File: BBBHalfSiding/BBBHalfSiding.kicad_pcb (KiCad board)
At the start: 2 copper layers, 54.6 x 86.4 mm, 2 parts, among them P8 BeagleBone_Black_Header, P9 BeagleBone_Black_Header

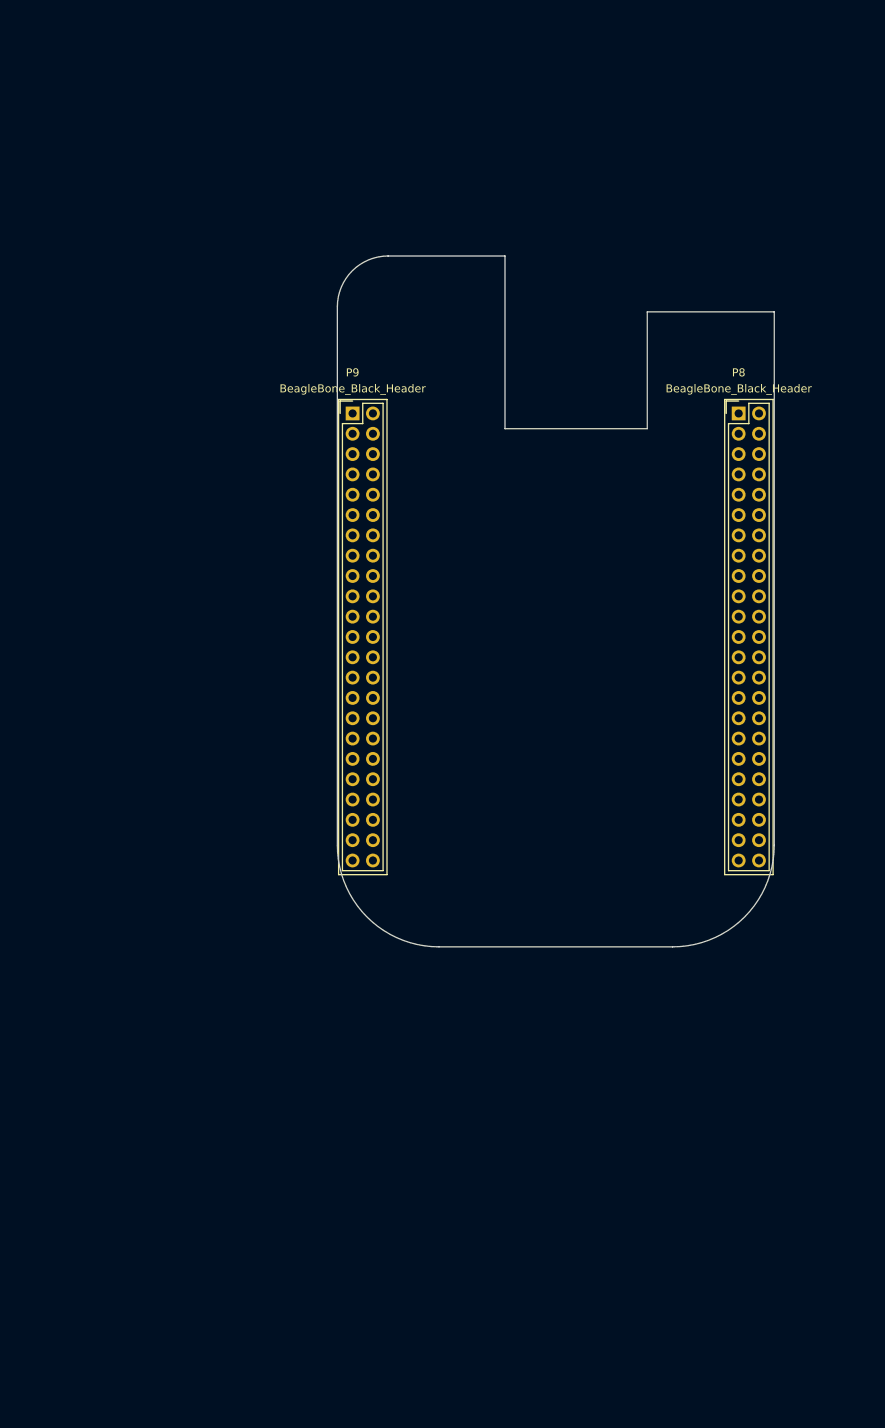
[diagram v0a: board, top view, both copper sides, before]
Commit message: Completed Beagle Bone Black Half Siding Cape
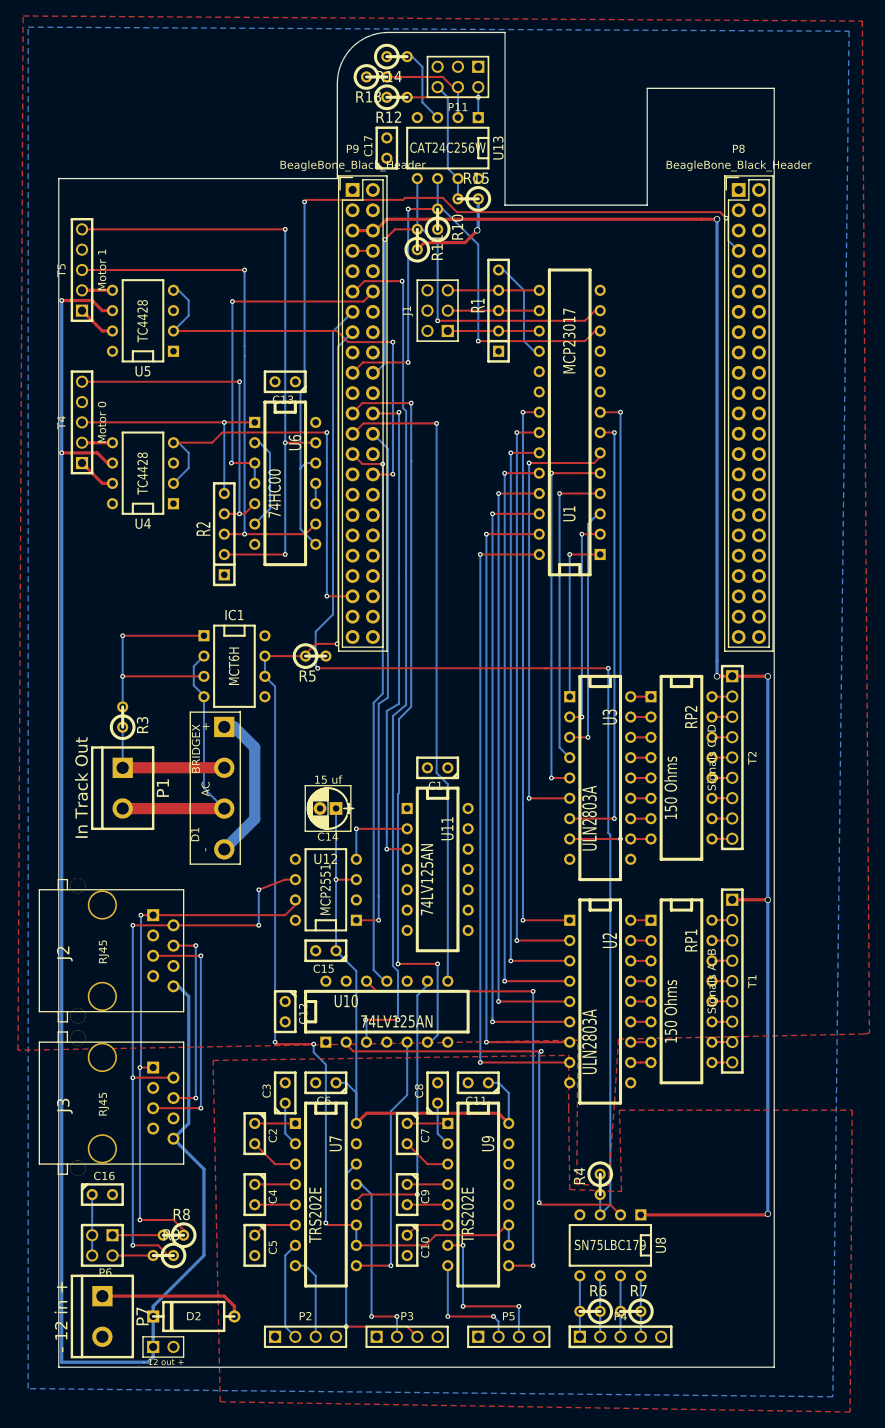
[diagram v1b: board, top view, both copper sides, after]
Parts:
- added C1: .1 uf, C1, F.Cu at (127.0, 106.7)
- added C10: .1 uf, C1, F.Cu at (123.2, 166.4)
- added C11: .1 uf, C1, F.Cu at (132.1, 146.1)
- added C12: .1 uf, C1, F.Cu at (108.0, 137.2)
- added C13: .1 uf, C1, F.Cu at (108.0, 58.4)
- added C14: 15 uf, CP_Radial_D5.0mm_P2.00mm, F.Cu at (114.3, 111.8)
- added C15: .1 uf, C1, F.Cu at (113.0, 129.5)
- added C16: 47 nf, C1, F.Cu at (85.1, 160.0)
- added C17: .1 uf, C1, F.Cu at (120.7, 29.2)
- added C2: .1 uf, C1, F.Cu at (104.1, 152.4)
- added C3: .1 uf, C1, F.Cu at (108.0, 147.3)
- added C4: .1 uf, C1, F.Cu at (104.1, 160.0)
- added C5: .1 uf, C1, F.Cu at (104.1, 166.4)
- added C6: .1 uf, C1, F.Cu at (113.0, 146.1)
- added C7: .1 uf, C1, F.Cu at (123.2, 152.4)
- added C8: .1 uf, C1, F.Cu at (127.0, 147.3)
- added C9: .1 uf, C1, F.Cu at (123.2, 160.0)
- added D1: BRIDGEX, KBL, F.Cu at (100.3, 109.2)
- added D2: SB240E, DO-15, F.Cu at (96.5, 175.3)
- added IC1: MCT6H, DIP-8__300, F.Cu at (101.6, 94.0)
- added J1: Address, pin_array_3x2, F.Cu at (127.0, 49.5)
- added J2: RJ45, RJ45_8N-S, F.Cu at (85.1, 129.5)
- added J3: RJ45, RJ45_8N-S, F.Cu at (85.1, 148.6)
- added P1: In Track Out, bornier2, F.Cu at (87.6, 109.2)
- added P10: - 12 out +, ScrewTerm2.54-2, F.Cu at (92.7, 179.1)
- added P11: addr / we, pin_array_3x2, F.Cu at (129.5, 20.3)
- added P2: East (Points), PIN_ARRAY_4x1, F.Cu at (110.5, 177.8)
- added P3: West Main (Frog, Normal), PIN_ARRAY_4x1, F.Cu at (123.2, 177.8)
- added P4: ABS Slave Bus, PIN_ARRAY_5x1, F.Cu at (149.9, 177.8)
- added P5: West Div. (Frog, Revesed), PIN_ARRAY_4x1, F.Cu at (135.9, 177.8)
- added P6: Termination, PIN_ARRAY_2X2, F.Cu at (85.1, 166.4)
- added P7: - 12 in +, bornier2, F.Cu at (85.1, 175.3)
- added R1: 10K Ohms, SIL-5, F.Cu at (134.6, 48.3)
- added R10: 5.6K Ohms, R1, F.Cu at (127.0, 38.1)
- added R11: 5.6K Ohms, R1, F.Cu at (124.5, 40.6)
- added R12: 4.75K Ohms, R1, F.Cu at (121.9, 22.9)
- added R13: 4.75K Ohms, R1, F.Cu at (119.4, 20.3)
- added R14: 4.75K Ohms, R1, F.Cu at (121.9, 17.8)
- added R15: 10K Ohms, R1, F.Cu at (130.8, 35.6)
- added R2: 10K Ohms, SIL-5, F.Cu at (100.3, 76.2)
- added R3: 10 Ohms, R1, F.Cu at (87.6, 100.3)
- added R4: 10K Ohms, R1, F.Cu at (147.3, 158.8)
- added R5: 10K Ohms, R1, F.Cu at (111.8, 92.7)
- added R6: 60 Ohms, R1, F.Cu at (146.1, 174.6)
- added R7: 60 Ohms, R1, F.Cu at (151.1, 174.6)
- added R8: 60 Ohms, R1, F.Cu at (94.0, 165.1)
- added R9: 60 Ohms, R1, F.Cu at (92.7, 167.6)
- added RP1: 150 Ohms, DIP-16__300, F.Cu at (157.5, 134.6)
- added RP2: 150 Ohms, DIP-16__300, F.Cu at (157.5, 106.7)
- added T1: Signals A, B, ScrewTerm_2.54-9, F.Cu at (163.8, 133.3)
- added T2: Signals C, D, ScrewTerm_2.54-9, F.Cu at (163.8, 105.4)
- added T4: Motor 0, ScrewTerm_2.54-5, F.Cu at (82.5, 63.5)
- added T5: Motor 1, ScrewTerm_2.54-5, F.Cu at (82.5, 44.5)
- added U1: MCP23017, DIP-28__300, F.Cu at (143.5, 63.5)
- added U10: 74LV125AN, DIP-14__300, F.Cu at (120.7, 137.2)
- added U11: 74LV125AN, DIP-14__300, F.Cu at (127.0, 119.4)
- added U12: MCP2551, DIP-8__300, F.Cu at (113.0, 121.9)
- added U13: CAT24C256W, DIP-8__300, F.Cu at (128.3, 29.2)
- added U2: ULN2803A, DIP-18__300, F.Cu at (147.3, 135.9)
- added U3: ULN2803A, DIP-18__300, F.Cu at (147.3, 108.0)
- added U4: TC4428, DIP-8__300, F.Cu at (90.2, 69.8)
- added U5: TC4428, DIP-8__300, F.Cu at (90.2, 50.8)
- added U6: 74HC00, DIP-14__300, F.Cu at (108.0, 71.1)
- added U7: TRS202E, DIP-16__300, F.Cu at (113.0, 160.0)
- added U8: SN75LBC179, DIP-8__300, F.Cu at (148.6, 166.4)
- added U9: TRS202E, DIP-16__300, F.Cu at (132.1, 160.0)
- moved P8 27.9 mm to (164.6, 34.4)
- moved P9 27.9 mm to (116.4, 34.4)
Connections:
- net +3V3 renamed +3.3V
- net GNDD renamed GND
- P8 pad 10: Net-(P8-Pad10) -> (no net)
- P8 pad 11: Net-(P8-Pad11) -> (no net)
- P8 pad 12: Net-(P8-Pad12) -> (no net)
- P8 pad 13: Net-(P8-Pad13) -> (no net)
- P8 pad 14: Net-(P8-Pad14) -> (no net)
- P8 pad 15: Net-(P8-Pad15) -> (no net)
- P8 pad 16: Net-(P8-Pad16) -> (no net)
- P8 pad 17: Net-(P8-Pad17) -> (no net)
- P8 pad 18: Net-(P8-Pad18) -> (no net)
- P8 pad 19: Net-(P8-Pad19) -> (no net)
- P8 pad 20: Net-(P8-Pad20) -> (no net)
- P8 pad 21: Net-(P8-Pad21) -> (no net)
- P8 pad 22: Net-(P8-Pad22) -> (no net)
- P8 pad 23: Net-(P8-Pad23) -> (no net)
- P8 pad 24: Net-(P8-Pad24) -> (no net)
- P8 pad 25: Net-(P8-Pad25) -> (no net)
- P8 pad 26: Net-(P8-Pad26) -> (no net)
- P8 pad 27: Net-(P8-Pad27) -> (no net)
- P8 pad 28: Net-(P8-Pad28) -> (no net)
- P8 pad 29: Net-(P8-Pad29) -> (no net)
- P8 pad 3: Net-(P8-Pad3) -> (no net)
- P8 pad 30: Net-(P8-Pad30) -> (no net)
- P8 pad 31: Net-(P8-Pad31) -> (no net)
- P8 pad 32: Net-(P8-Pad32) -> (no net)
- P8 pad 33: Net-(P8-Pad33) -> (no net)
- P8 pad 34: Net-(P8-Pad34) -> (no net)
- P8 pad 35: Net-(P8-Pad35) -> (no net)
- P8 pad 36: Net-(P8-Pad36) -> (no net)
- P8 pad 37: Net-(P8-Pad37) -> (no net)
- P8 pad 38: Net-(P8-Pad38) -> (no net)
- P8 pad 39: Net-(P8-Pad39) -> (no net)
- P8 pad 4: Net-(P8-Pad4) -> (no net)
- P8 pad 40: Net-(P8-Pad40) -> (no net)
- P8 pad 41: Net-(P8-Pad41) -> (no net)
- P8 pad 42: Net-(P8-Pad42) -> (no net)
- P8 pad 43: Net-(P8-Pad43) -> (no net)
- P8 pad 44: Net-(P8-Pad44) -> (no net)
- P8 pad 45: Net-(P8-Pad45) -> (no net)
- P8 pad 46: Net-(P8-Pad46) -> (no net)
- P8 pad 5: Net-(P8-Pad5) -> (no net)
- P8 pad 6: Net-(P8-Pad6) -> (no net)
- P8 pad 7: Net-(P8-Pad7) -> /M1_Sense
- P8 pad 8: Net-(P8-Pad8) -> (no net)
- P8 pad 9: Net-(P8-Pad9) -> (no net)
- P9 pad 10: SYS_RESETN -> (no net)
- P9 pad 11: Net-(P9-Pad11) -> /Sensors/RX
- P9 pad 12: Net-(P9-Pad12) -> /M0_Sense
- P9 pad 13: Net-(P9-Pad13) -> /Sensors/TX
- P9 pad 14: Net-(P9-Pad14) -> (no net)
- P9 pad 15: Net-(P9-Pad15) -> /Sensors/Occupancy
- P9 pad 16: Net-(P9-Pad16) -> (no net)
- P9 pad 17: Net-(P9-Pad17) -> (no net)
- P9 pad 18: Net-(P9-Pad18) -> (no net)
- P9 pad 19: Net-(P9-Pad19) -> /Signals/SCL
- P9 pad 20: Net-(P9-Pad20) -> /Signals/SDA
- P9 pad 21: Net-(P9-Pad21) -> (no net)
- P9 pad 22: Net-(P9-Pad22) -> (no net)
- P9 pad 23: Net-(P9-Pad23) -> /Sensors/East (Points) Occ
- P9 pad 24: Net-(P9-Pad24) -> /CANBUSDriver/CANRX
- P9 pad 25: Net-(P9-Pad25) -> /Sensors/West Main (Frog Normal) Occ
- P9 pad 26: Net-(P9-Pad26) -> /CANBUSDriver/CANTX
- P9 pad 27: Net-(P9-Pad27) -> /Sensors/West Diverg (Frog Reversed) Occ
- P9 pad 28: Net-(P9-Pad28) -> (no net)
- P9 pad 29: Net-(P9-Pad29) -> (no net)
- P9 pad 30: Net-(P9-Pad30) -> /M1_Control
- P9 pad 31: Net-(P9-Pad31) -> (no net)
- P9 pad 32: VDD_ADC -> (no net)
- P9 pad 33: Net-(P9-Pad33) -> (no net)
- P9 pad 34: GNDA_ADC -> (no net)
- P9 pad 35: Net-(P9-Pad35) -> (no net)
- P9 pad 36: Net-(P9-Pad36) -> (no net)
- P9 pad 37: Net-(P9-Pad37) -> (no net)
- P9 pad 38: Net-(P9-Pad38) -> (no net)
- P9 pad 39: Net-(P9-Pad39) -> (no net)
- P9 pad 40: Net-(P9-Pad40) -> (no net)
- P9 pad 41: Net-(P9-Pad41) -> /M0_Control
- P9 pad 42: Net-(P9-Pad42) -> (no net)
- P9 pad 9: PWR_BUT -> (no net)
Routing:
- net +5V: track 0.00 -> 274.3 mm, vias 0 -> 6
- net +12V: track 0.00 -> 210.7 mm, vias 0 -> 2
- net /Sensors/Occupancy: track 0.00 -> 155.4 mm, vias 0 -> 4
- net /Sensors/TX: track 0.00 -> 154.4 mm, vias 0 -> 2
- net /Sensors/RX: track 0.00 -> 107.3 mm, vias 0 -> 3
- net /M1_Sense: track 0.00 -> 104.8 mm, vias 0 -> 2
- net /Sensors/East (Points) Occ: track 0.00 -> 94.6 mm, vias 0 -> 3
- net /Signals/GP0-7: track 0.00 -> 82.0 mm, vias 0 -> 2
- net /Sensors/West Main (Frog Normal) Occ: track 0.00 -> 81.3 mm, vias 0 -> 1
- net /Signals/GP0-6: track 0.00 -> 80.5 mm, vias 0 -> 2
- net /Signals/GP0-5: track 0.00 -> 79.0 mm, vias 0 -> 2
- net N-0000072: track 0.00 -> 77.5 mm, vias 0 -> 3
- net /Signals/GP0-4: track 0.00 -> 77.5 mm, vias 0 -> 2
- net /Signals/GP0-3: track 0.00 -> 75.9 mm, vias 0 -> 2
- net N-00000206: track 0.00 -> 75.7 mm, vias 0 -> 5
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- added copper zone on F.Cu, net +3.3V
- added copper zone on F.Cu, net +5V
- added copper zone on B.Cu, net GND
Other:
- board size 54.6 x 86.4 mm -> 89.4 x 166.9 mm

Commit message: Updates to BBBHalfSiding (silk screen tweaks)
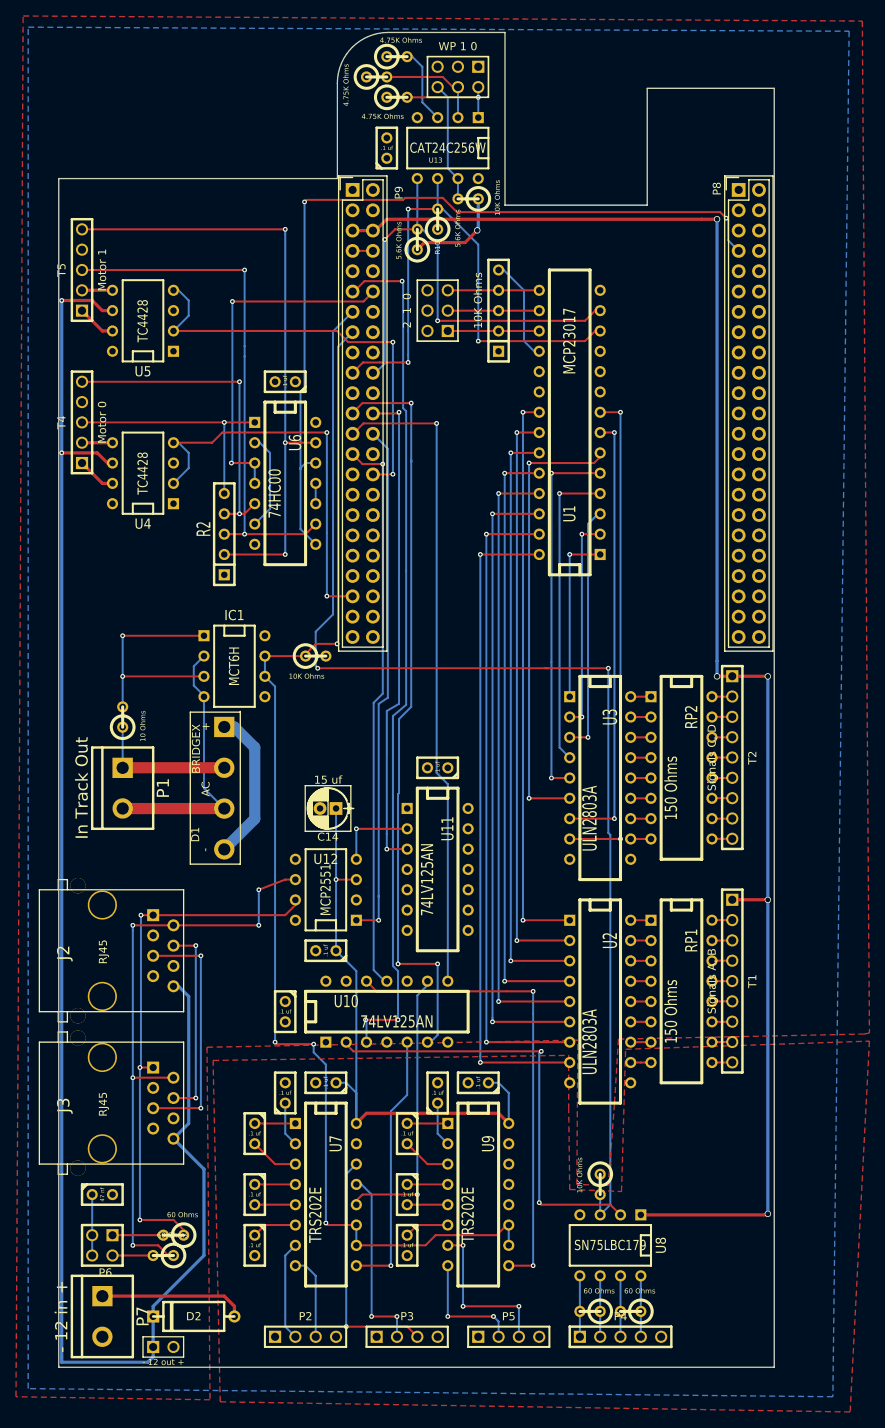
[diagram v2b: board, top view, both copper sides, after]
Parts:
- J1: value Address -> 2 1 0
- P11: value addr / we -> WP 1 0

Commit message: Add missing bypass caps.
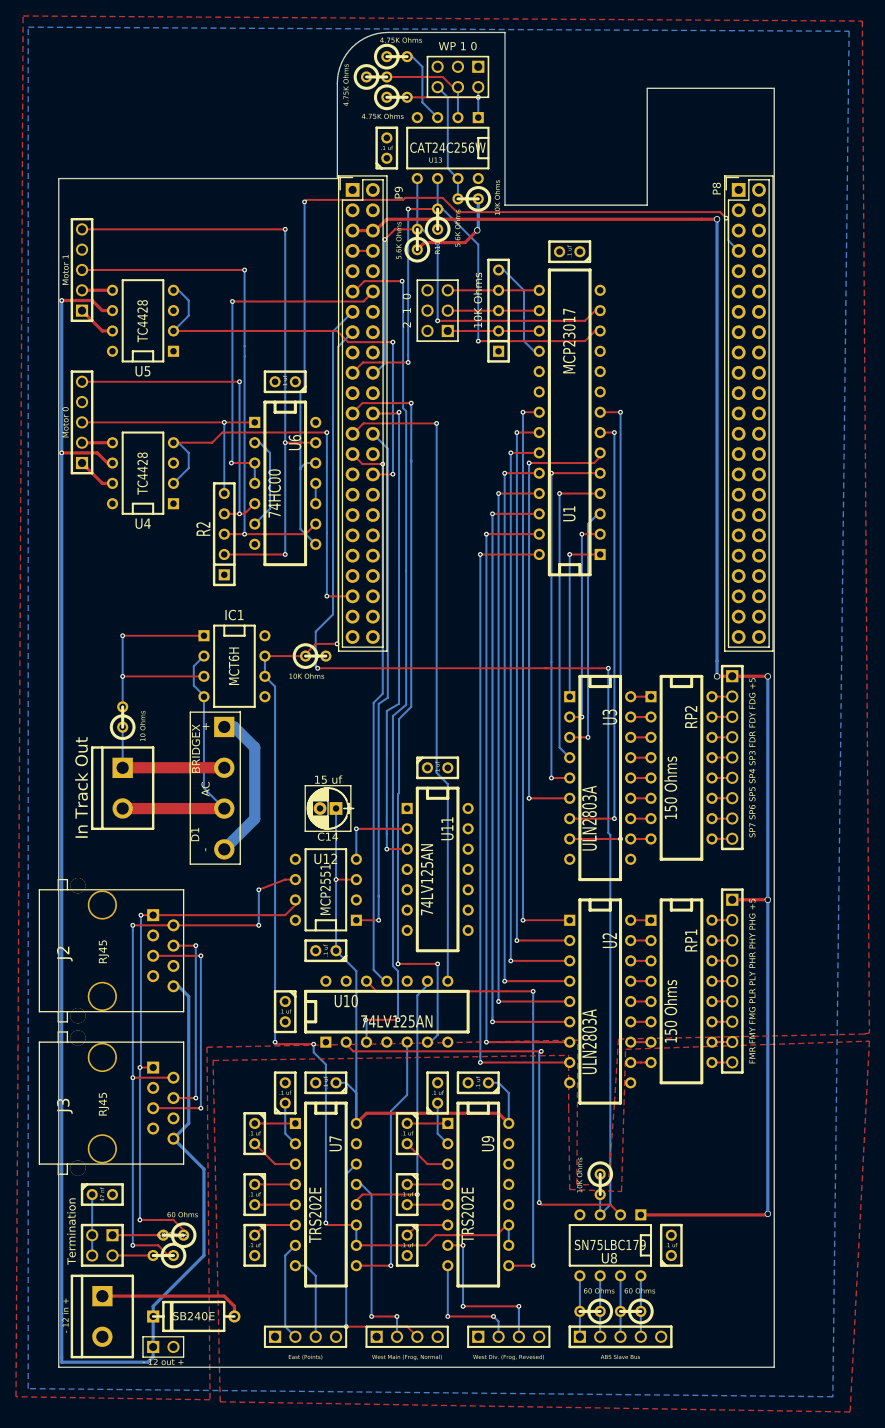
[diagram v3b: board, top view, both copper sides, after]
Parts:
- added C18: .1 uf, C1, F.Cu at (156.2, 166.4)
- added C19: .1 uf, C1, F.Cu at (127.0, 106.7)
- T1: value Signals A, B -> FMR FMY FMG PLR PLY PHR PHY PHG +5
- T2: value Signals C, D -> SP7 SP6 SP5 SP4 SP3 FDR FDY FDG +5
- moved C1 66.6 mm to (143.5, 42.2)

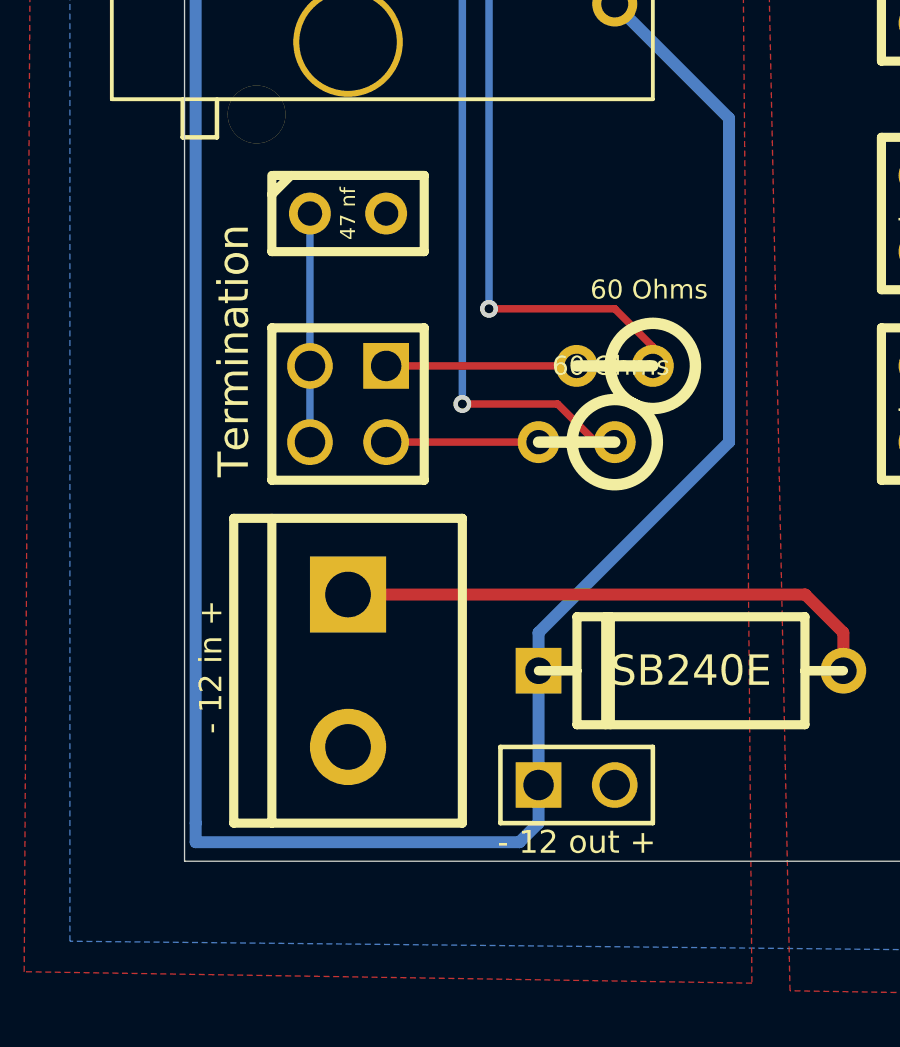
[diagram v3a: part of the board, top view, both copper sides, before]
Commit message: Tweaks to the silk screen for BBBHalfSiding cape.
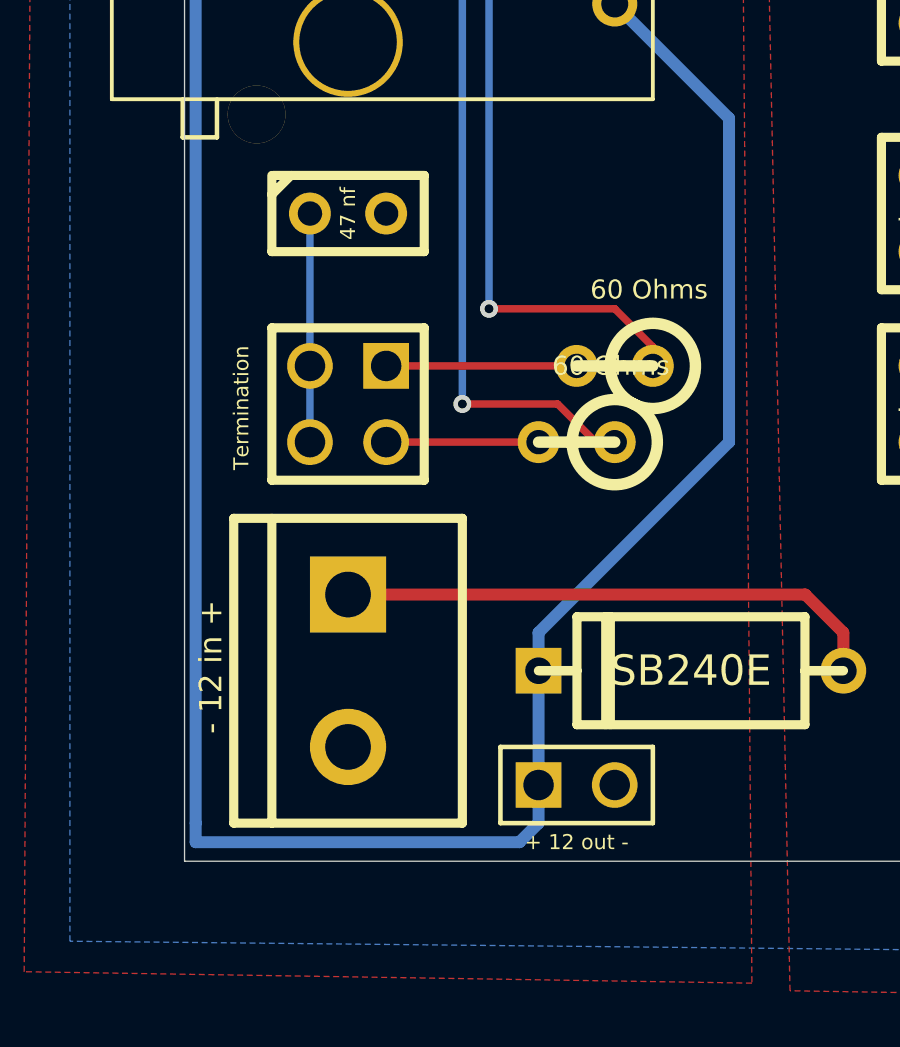
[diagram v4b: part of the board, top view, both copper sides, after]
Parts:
- P10: value - 12 out + -> + 12 out -
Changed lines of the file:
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@@
       (effects (font (size 0.762 0.762) (thickness 0.1524)))
     )
-    (fp_text value "- 12 out +" (at 0 1.905) (layer F.SilkS)
-      (effects (font (size 0.762 0.762) (thickness 0.1524)))
+    (fp_text value "+ 12 out -" (at 0 1.905) (layer F.SilkS)
+      (effects (font (size 0.5 0.5) (thickness 0.1016)))
     )
     (fp_line (start -2.54 1.27) (end -2.54 -1.27) (layer F.SilkS) (width 0.1524))
@@
       (effects (font (size 1.016 1.016) (thickness 0.2032)))
     )
-    (fp_text value Termination (at 3.81 1.778 270) (layer F.SilkS)
-      (effects (font (size 1.016 1.016) (thickness 0.2032)))
+    (fp_text value Termination (at 3.556 -0.127 270) (layer F.SilkS)
+      (effects (font (size 0.5 0.5) (thickness 0.1016)))
     )
     (fp_line (start -2.54 -2.54) (end 2.54 -2.54) (layer F.SilkS) (width 0.3048))
